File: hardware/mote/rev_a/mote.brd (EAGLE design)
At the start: 160 x 100 mm, 139 parts, among them J1 TC2030-JLINK-L, J2 TC2030-JLINK-NL, Q1 CSD22206W, Q10 CSD22206W, Q11 CSD22206W, Q2 CSD22206W, Q6 CSD22206W, Q7 CSD22206W, Q8 CSD22206W, Q9 CSD22206W, U1 NRF52840, U10 MS5637-02BA03, U11 ADP5091, U12 NRF51822QF, U3 MAX17222, U4 AMN41121, U5 SI7021-A20-GM1, U6 ISL29125, U7 MAX44009, U8 LIS2DW12, U9 AB1815-T3, X1 7V-32.000MAHV-T, X2 ABS05-32.768KHZ-9-T, X3 ABS07-32.768KHZ-7-T, X5 16MHz, X6 ABS05-32.768KHZ-9-T

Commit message: rearrange and combine power ics
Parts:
- moved J1 155.3 mm to (-82.5, 59.6)
- moved C30 85.7 mm to (-2.16, 122.6)
- moved X1 85.7 mm to (8.51, 128.3)
- moved A3 85.7 mm to (19.6, 130.4)
- moved B2 85.7 mm to (22.1, 126.9)
- moved C1 85.7 mm to (5.97, 128.4)
- moved C11 85.7 mm to (8.46, 125.2)
- moved C12 85.7 mm to (5.84, 126.7)
- moved C14 85.7 mm to (-1.91, 126.0)
- moved C15 85.7 mm to (1.65, 126.2)
- moved C2 85.7 mm to (10.8, 128.4)
- moved C29 85.7 mm to (1.65, 127.8)
- moved C3 85.7 mm to (7.37, 123.2)
- moved C31 85.7 mm to (-3.56, 123.8)
- moved C4 85.7 mm to (9.78, 123.3)
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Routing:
- net VBAT: track 121.7 -> 79.7 mm
- net SW: track 21.3 -> 2.13 mm
- net VOUT1: track 13.2 -> 0.00 mm
- net VSEC: track 9.92 -> 21.3 mm, vias 0 -> 1
- net N$14: track 7.28 -> 1.95 mm
- net VSW: track 12.7 -> 8.45 mm
- net N$47: track 2.05 -> 3.05 mm
- added copper zone on layer 1, net VCC
- added copper zone on layer 1, net VSW
- removed copper zone on layer 1, net VBATT
- removed copper zone on layer 1, net VOUT1
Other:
- board text removed: "DISABLE"
- board text removed: "ENABLE"

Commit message: Connect up nrf51822, wire up sensors
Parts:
- removed A3: FRACTUS-2.4GHZ-FR05-S1-N-0-102, chips:FRACTUS-ANTENNA-FR05-S1-N-0-102
- added A2: ANT3216A063R2400A, chips:ANT3216A063R2400A
- A1: value FRACTUS-2.4GHZ-FR05-S1-N-0-102 -> ANT3216A063R2400A; device chips:FRACTUS-ANTENNA-FR05-S1-N-0-102 -> chips:ANT3216A063R2400A
- J2: value TC2030-JLINK-NL -> TC2030-JLINK-L; device connector:TC2030-IDC-NL -> connector:TC2030-IDC
- moved R25 665.6 mm to (22.4, 75.4)
- moved Q2 658.4 mm to (23.4, 71.4)
- moved Q1 654.2 mm to (21.3, 71.4)
- moved R24 596.3 mm to (10.2, 19.8), turned to 90 degrees
- moved R23 594.3 mm to (20.8, 19.1), turned to 270 degrees
- moved TP27 517.1 mm to (-9.91, 69.3)
- moved TP26 508.9 mm to (-11.4, 76.5)
- moved TP25 507.7 mm to (26.2, 82.8)
- moved R14 506.7 mm to (13.7, 8.89), turned to 180 degrees
- moved Q11 505.0 mm to (14.0, 7.11)
- moved JP7 499.6 mm to (17.5, 83.8)
- moved TP29 496.8 mm to (16.8, 9.40), turned to 270 degrees
- moved TP24 492.6 mm to (20.6, 83.8)
- moved JP8 486.4 mm to (16.8, 6.35), turned to 90 degrees
- moved TP28 476.0 mm to (16.8, 3.05), turned to 270 degrees
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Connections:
- removed net N$38: C28.1, D1.+, L2.P$2, R22.2, TP1.TESTPOINT, U11.10
- new net VSOL: C28.1, D1.+, L2.P$2, R22.2, TP1.TESTPOINT, U1.A10, U11.10, U12.7
- net !ACC_EN: now also U12.22
- net !CLR_EN: now also U12.26
- net !CLR_INT: now also U12.48
- net !HUM_EN: now also U12.40
- net !I2C_EN: now also U12.21
- net !LT_EN: now also U12.25
- net !LT_INT: now also U12.47
- net !PIR_EN: now also U12.27
- net !PR_EN: now also U12.28
- net !RTC_IRQ1: now also U12.41
- net !RTC_IRQ2: now also U12.42
- net ACC_CS: now also U12.19
- net ACC_INT1: now also U12.43
- net ACC_INT2: now also U12.44
- net GND: now also A1.S2, A2.S2
- net MISO: now also U12.16
- net MOSI: now also U12.17
- net N$6: now also A2.S1; no longer A1.1
- net N$62: now also A1.S1; no longer A3.1
- net PIR_OUT: now also U12.3
- net RTC_CS: now also U12.20
- net SCK: now also U12.18
- net SCL: now also U12.15
- net SDA: now also U12.14
- net SW: now also U12.11; no longer U1.J1
- net VBAT: now also U1.J1, U12.6; no longer U1.A10
- net VSEC: now also U12.5
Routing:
- net VBAT: track 79.7 -> 7.26 mm
- net SDA: track 1.46 -> 54.5 mm, vias 0 -> 2
- net SCL: track 1.46 -> 52.9 mm, vias 0 -> 2
- net N$37: track 0.00 -> 20.1 mm, vias 0 -> 2
- net N$33: track 0.00 -> 17.9 mm
- net VSEC: track 21.3 -> 4.57 mm, vias 1 -> 0
- net VCC: track 0.00 -> 16.2 mm
- net N$40: track 0.00 -> 13.1 mm
- net N$19: track 0.00 -> 12.1 mm
- net VSOL: track 0.00 -> 11.4 mm
- net N$38: track 11.4 -> 0.00 mm
- net N$36: track 0.00 -> 11.2 mm
- net N$24: track 0.00 -> 10.8 mm
- net N$23: track 0.00 -> 10.0 mm
- net MISO: track 2.96 -> 10.7 mm
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- added copper zone on layer 1, net N$38
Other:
- board text added: "Acceleration"
- board text added: "Color"
- board text added: "Humidity"
- board text added: "Light"
- board text added: "Occupancy"
- board text added: "Pressure"

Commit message: change to 4lyr
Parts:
- moved A1 73.9 mm to (-3.11, 60.3)
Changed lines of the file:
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@@
 <layers>
 <layer number="1" name="Top" color="4" fill="1" visible="yes" active="yes"/>
-<layer number="2" name="Route2" color="1" fill="3" visible="no" active="no"/>
+<layer number="2" name="Route2" color="1" fill="3" visible="no" active="yes"/>
 <layer number="3" name="Route3" color="4" fill="3" visible="no" active="no"/>
 <layer number="4" name="Route4" color="1" fill="4" visible="no" active="no"/>
@@
 <layer number="13" name="Route13" color="4" fill="5" visible="no" active="no"/>
 <layer number="14" name="Route14" color="1" fill="6" visible="no" active="no"/>
-<layer number="15" name="Route15" color="4" fill="6" visible="no" active="no"/>
+<layer number="15" name="Route15" color="4" fill="6" visible="no" active="yes"/>
 <layer number="16" name="Bottom" color="1" fill="1" visible="yes" active="yes"/>
 <layer number="17" name="Pads" color="2" fill="1" visible="yes" active="yes"/>
@@
 </class>
 </classes>
-<designrules name="quickturn_co_kr_1oz">
-<description language="en">&lt;b&gt;EAGLE Design Rules for *2* Layer Designs (DS)&lt;/b&gt;
+<designrules name="quickturn_co_kr_1oz_4lyr">
+<description language="en">&lt;b&gt;EAGLE Design Rules for *4* Layer Designs (DS)&lt;/b&gt;
 &lt;p&gt;
-This Sunstone Circuits 2 Layer .DRU has been set to cover our minimum requirements for our double sided products. For questions, comments, suggestions, please contact Sunstone Customer Support: &lt;p&gt;&lt;b&gt;Email:&lt;/b&gt;  mailto:support@sunstone.com&lt;br&gt;&lt;b&gt;Phone:&lt;/b&gt; 800-228-8198.&lt;p&gt; v1.1Mod10/16/07~Layers-core reversal.Distance C/D.Restring%.Supply G%.&lt;p&gt; v1.2 Mod12/06/07~Distance C/D to 20mils.&lt;p&gt;v1.3Mod12/12/07~Supply/Annulus Value to 12.5mils&lt;p&gt;1/15/08 SSC-EAGLE-2Lyr_v1.0.0.3~For Release&lt;p&gt;10/3/08 Description Edit.&lt;p&gt;
-&lt;p&gt;
-&lt;i&gt;Attention: Upon running the design check and making modifications, please remember to save any changes before closing the application and sending in your board file to Sunstone Circuits for conversion.&lt;i&gt;</description>
-<param name="layerSetup" value="(1*16)"/>
+Quickturn PCB 4 Layer .DRU</description>
+<param name="layerSetup" value="(1+2*15+16)"/>
 <param name="mtCopper" value="0.0178mm 0.0356mm 0.0356mm 0.0356mm 0.0356mm 0.0356mm 0.0356mm 0.0356mm 0.0356mm 0.0356mm 0.0356mm 0.0356mm 0.0356mm 0.0356mm 0.0356mm 0.0178mm"/>
 <param name="mtIsolate" value="59mil 0.1499mm 0.2007mm 0.1499mm 0.2007mm 0.1499mm 0.2007mm 0.1499mm 0.2007mm 0.1499mm 0.2007mm 0.1499mm 0.2007mm 0.1499mm 0.2007mm"/>
@@
 <param name="mdDrill" value="12mil"/>
 <param name="mdSmdStop" value="0mil"/>
-<param name="msWidth" value="4mil"/>
-<param name="msDrill" value="0.200659375mm"/>
-<param name="msMicroVia" value="9.9898mm"/>
+<param name="msWidth" value="6mil"/>
+<param name="msDrill" value="8mil"/>
+<param name="msMicroVia" value="4mil"/>
 <param name="msBlindViaRatio" value="0.5"/>
 <param name="rvPadTop" value="0.25"/>
@@
 <attribute name="NAME" x="5.052" y="97.29" size="1.016" layer="21" font="vector" ratio="12" rot="R180"/>
 </element>
-<element name="A1" library="chips" package="ANT3216A063R2400A" value="ANT3216A063R2400A" x="-22.606" y="-10.922" smashed="yes">
-<attribute name="DIGIKEY" value="311-1542-1-ND" x="-28.194" y="-4.826" size="1.016" layer="27" font="vector" ratio="12" display="off"/>
-<attribute name="MANUFACTURER" value="YAGEO" x="-28.194" y="-4.826" size="1.016" layer="27" font="vector" ratio="12" display="off"/>
-<attribute name="MPN" value="ANT3216A063R2400A" x="-28.194" y="-4.826" size="1.016" layer="27" font="vector" ratio="12" display="off"/>
-<attribute name="NAME" x="-24.106" y="-9.672" size="1.016" layer="21" font="vector" ratio="12"/>
+<element name="A1" library="chips" package="ANT3216A063R2400A" value="ANT3216A063R2400A" x="-3.106" y="60.328" smashed="yes">
+<attribute name="DIGIKEY" value="311-1542-1-ND" x="-8.694" y="66.424" size="1.016" layer="27" font="vector" ratio="12" display="off"/>
+<attribute name="MANUFACTURER" value="YAGEO" x="-8.694" y="66.424" size="1.016" layer="27" font="vector" ratio="12" display="off"/>
+<attribute name="MPN" value="ANT3216A063R2400A" x="-8.694" y="66.424" size="1.016" layer="27" font="vector" ratio="12" display="off"/>
+<attribute name="NAME" x="-4.606" y="61.578" size="1.016" layer="21" font="vector" ratio="12"/>
 </element>
 </elements>
@@
 <wire x1="5.592" y1="42.049" x2="5.092" y2="42.049" width="0" layer="19" extent="1-1"/>
 <wire x1="18.923" y1="40.767" x2="16.51" y2="43.99406875" width="0" layer="19" extent="1-1"/>
-<wire x1="-11.43" y1="76.454" x2="4.588" y2="80.97393125" width="0" layer="19" extent="1-1"/>
-<wire x1="-9.906" y1="69.342" x2="-11.43" y2="76.454" width="0" layer="19" extent="1-1"/>
-<wire x1="-21.281" y1="-10.922" x2="8.908" y2="8.146" width="0" layer="19" extent="1-1"/>
+<wire x1="-1.781" y1="60.328" x2="4.5692" y2="59.07913125" width="0" layer="19" extent="1-1"/>
+<wire x1="-9.906" y1="69.342" x2="-1.781" y2="60.328" width="0" layer="19" extent="1-1"/>
+<wire x1="-11.43" y1="76.454" x2="-9.906" y2="69.342" width="0" layer="19" extent="1-1"/>
 </signal>
 <signal name="N$8">
@@
 <wire x1="4.57046875" y1="60.198" x2="2.423" y2="60.198" width="1.27" layer="1"/>
 <contactref element="A1" pad="S1"/>
-<wire x1="-23.931" y1="-10.922" x2="2.423" y2="60.198" width="0" layer="19" extent="1-1"/>
+<wire x1="-4.431" y1="60.328" x2="2.423" y2="60.198" width="0" layer="19" extent="1-1"/>
 </signal>
 <signal name="AVDD1">
@@
 <contactref element="U1" pad="T2"/>
 <via x="10.1506" y="83.6803" extent="1-16" drill="0.2032"/>
-<wire x1="9.652" y1="83.737" x2="10.0939" y2="83.737" width="0.1016" layer="1"/>
-<wire x1="10.0939" y1="83.737" x2="10.1506" y2="83.6803" width="0.1016" layer="1"/>
 <contactref element="R10" pad="1"/>
 <contactref element="Q7" pad="A1"/>
@@
 <wire x1="15.248" y1="19.804" x2="15.248" y2="21.77706875" width="0.2032" layer="1"/>
 <wire x1="15.248" y1="21.77706875" x2="15.31493125" y2="21.844" width="0.2032" layer="1"/>
+<wire x1="9.652" y1="83.737" x2="10.0939" y2="83.737" width="0.1016" layer="1"/>
+<wire x1="10.0939" y1="83.737" x2="10.1506" y2="83.6803" width="0.1016" layer="1"/>
 <wire x1="7.4152" y1="62.398" x2="10.938" y2="82.042" width="0" layer="19" extent="1-1"/>
 <wire x1="15.31493125" y1="21.844" x2="7.4152" y2="62.398" width="0" layer="19" extent="1-1"/>

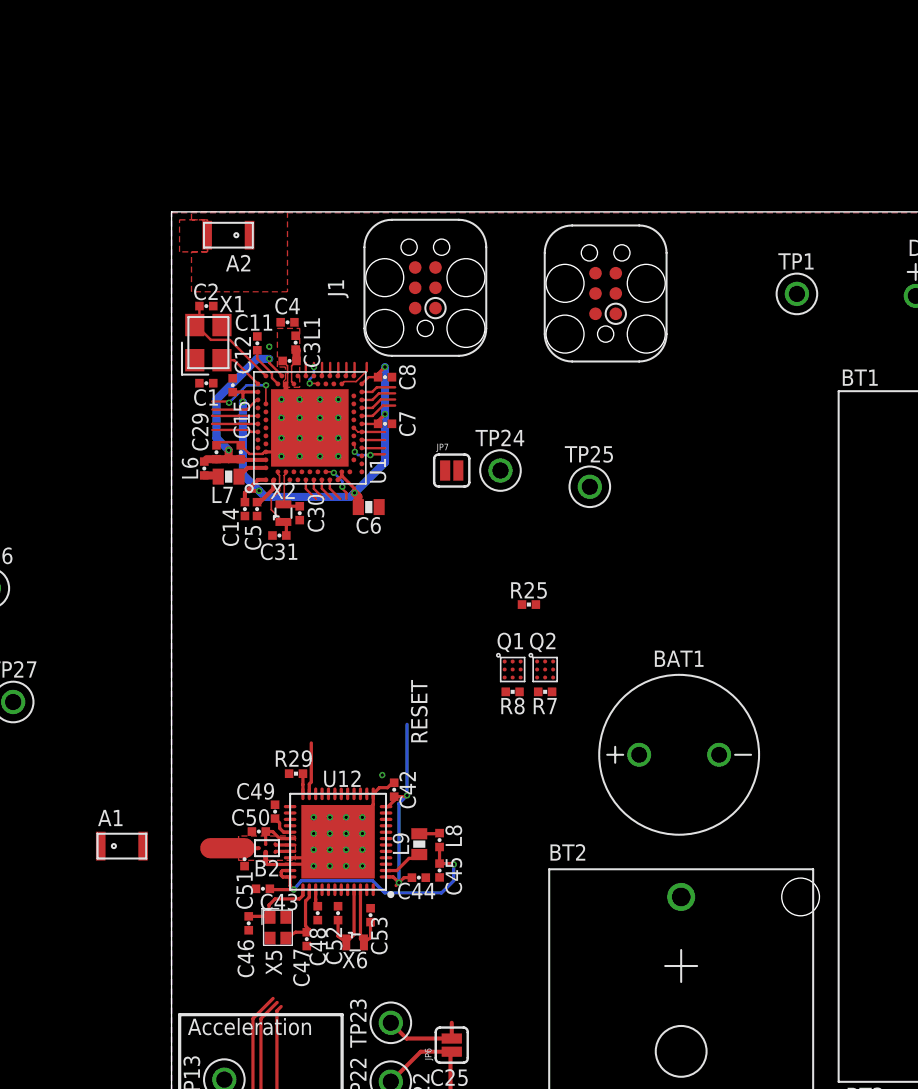
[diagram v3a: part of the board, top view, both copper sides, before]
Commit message: Antenna Layout
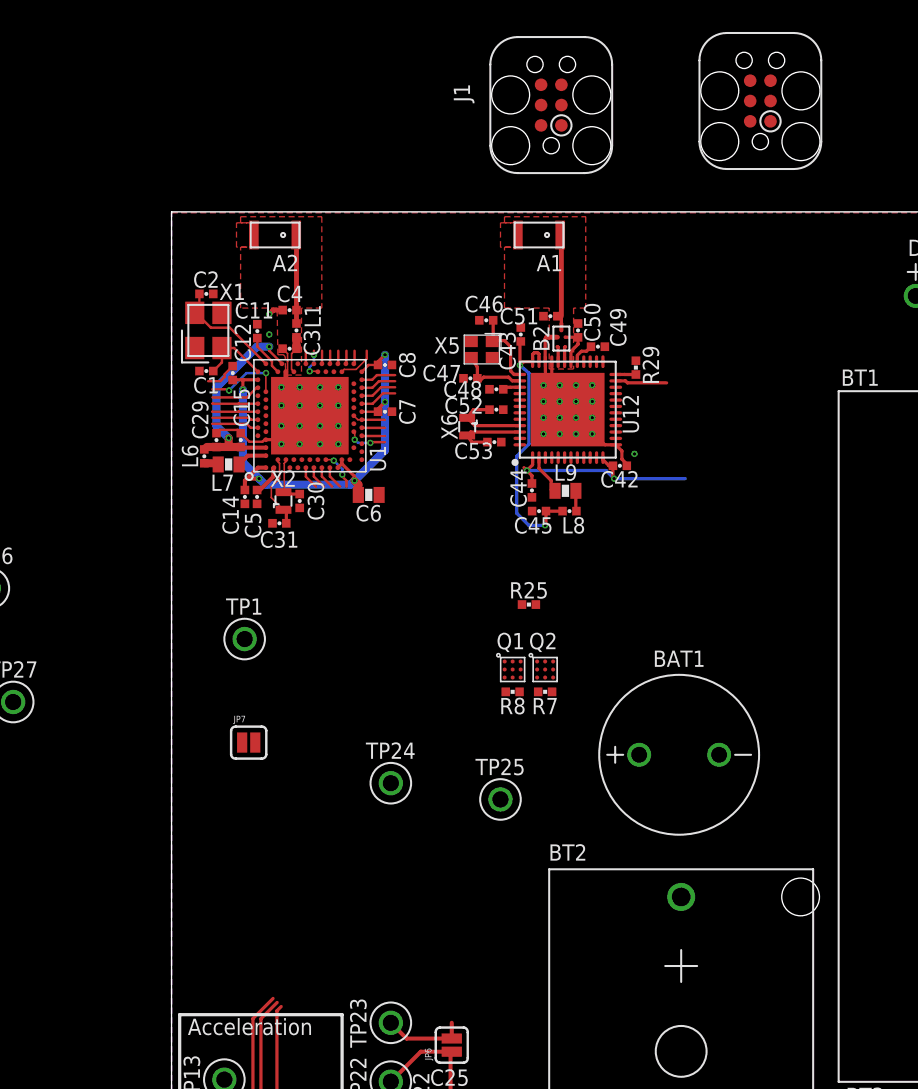
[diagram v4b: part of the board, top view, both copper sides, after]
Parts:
- moved A1 46.3 mm to (23.0, 98.6), turned to 180 degrees
- moved TP1 40.7 mm to (4.57, 73.3)
- moved C46 40.5 mm to (19.7, 93.2), turned to 180 degrees
- moved C51 39.0 mm to (23.7, 93.5), turned to 180 degrees
- moved X5 38.4 mm to (19.4, 91.4), turned to 180 degrees
- moved C43 38.2 mm to (21.8, 92.3), turned to 90 degrees
- moved C50 37.2 mm to (25.4, 92.6), turned to 90 degrees
- moved B2 36.8 mm to (24.4, 92.1), turned to 90 degrees
- moved C47 36.5 mm to (18.7, 89.6), turned to 180 degrees
- moved C49 35.4 mm to (26.7, 91.6), turned to 0 degrees
- moved C48 34.6 mm to (20.3, 88.9), turned to 180 degrees
- moved R29 33.1 mm to (29.0, 90.3), turned to 90 degrees
- moved C52 33.0 mm to (20.3, 87.6), turned to 0 degrees
- moved X6 33.0 mm to (18.5, 86.6), turned to 270 degrees
- moved U12 30.6 mm to (24.8, 87.6), turned to 90 degrees
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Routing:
- net N$6: track 0.00 -> 5.54 mm
- net VSOL: track 11.4 -> 14.3 mm
- net GND: track 30.4 -> 33.3 mm, vias 53 -> 54
- net N$62: track 3.28 -> 5.99 mm
- net N$9: track 2.86 -> 4.53 mm
- removed copper zone on layer 1, net N$35
- removed copper zone on layer 1, net N$7
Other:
- board text removed: "RESET"
